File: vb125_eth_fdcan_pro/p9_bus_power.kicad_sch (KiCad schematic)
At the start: 44 parts, among them T2 750315125, U14 LV14360SDDAR, U15 LT8304IS8E#PBF

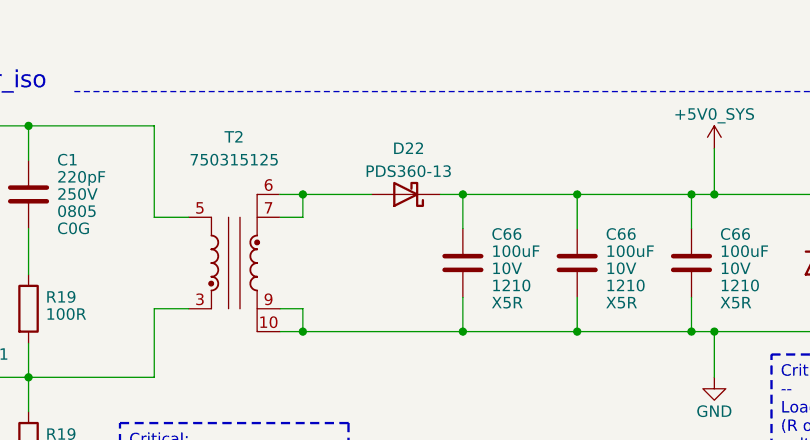
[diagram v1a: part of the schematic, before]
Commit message: Preliminary placement.
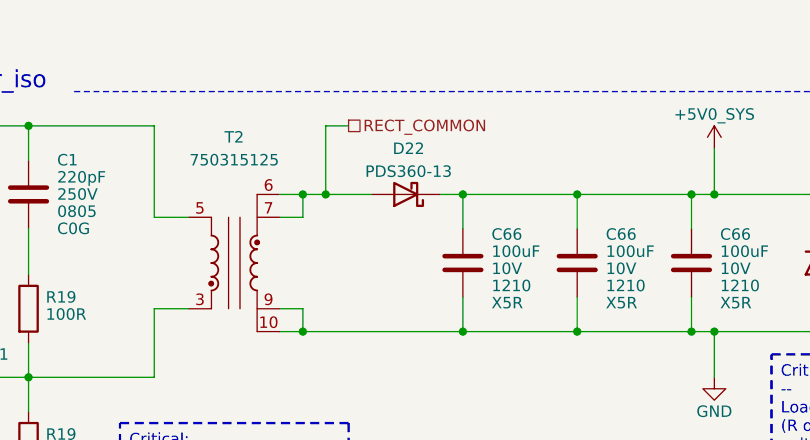
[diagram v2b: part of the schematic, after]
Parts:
- C66, D22: Variant bp_iso -> bp_iso or poe
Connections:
- net RECT_COMMON: now reaches D22.2 (A), T2.6, T2.7
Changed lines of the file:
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@@
   (junction (at 200.66 110.49) (diameter 0) (color 0 0 0 0)
+  )
+  (junction (at 254 73.66) (diameter 0) (color 0 0 0 0)
   )
   (junction (at 251.46 73.66) (diameter 0) (color 0 0 0 0)
@@
     (stroke (width 0) (type default))
   )
+  (wire (pts (xy 254 73.66) (xy 259.08 73.66))
+    (stroke (width 0) (type default))
+  )
   (wire (pts (xy 209.55 110.49) (xy 209.55 119.38))
     (stroke (width 0) (type default))
@@
     (stroke (width 0) (type default))
   )
+  (wire (pts (xy 256.54 66.04) (xy 254 66.04))
+    (stroke (width 0) (type default))
+  )
   (wire (pts (xy 281.94 88.9) (xy 269.24 88.9))
     (stroke (width 0) (type default))
@@
     (stroke (width 0) (type default))
   )
-  (wire (pts (xy 251.46 73.66) (xy 259.08 73.66))
+  (wire (pts (xy 251.46 73.66) (xy 254 73.66))
     (stroke (width 0) (type default))
   )
@@
   )
   (wire (pts (xy 251.46 86.36) (xy 251.46 88.9))
+    (stroke (width 0) (type default))
+  )
+  (wire (pts (xy 254 66.04) (xy 254 73.66))
     (stroke (width 0) (type default))
   )
@@
     (effects (font (size 1.27 1.27)) (justify right))
   )
+  (hierarchical_label "RECT_COMMON" (shape passive) (at 256.54 66.04 0) (fields_autoplaced)
+    (effects (font (size 1.27 1.27)) (justify left))
+    (property "Intersheetrefs" "${INTERSHEET_REFS}" (at 272.123 66.04 0)
+      (effects (font (size 1.27 1.27)) (justify left) hide)
+    )
+  )
   (symbol (lib_id "vhrd_power:+5V0_SYS") (at 297.18 68.58 0) (unit 1)
     (in_bom yes) (on_board yes) (dnp no) (fields_autoplaced)
@@
       (effects (font (size 1.27 1.27)) hide)
     )
-    (property "Variant" "bp_iso" (at 262.89 73.66 0)
+    (property "Variant" "bp_iso or poe" (at 262.89 73.66 0)
       (effects (font (size 1.27 1.27)) hide)
     )
@@
       (effects (font (size 1.27 1.27)) (justify left))
     )
-    (property "Variant" "bp_iso" (at 294.64 81.28 0)
+    (property "Variant" "bp_iso or poe" (at 294.64 81.28 0)
       (effects (font (size 1.27 1.27)) hide)
     )
@@
       (effects (font (size 1.27 1.27)) (justify left))
     )
-    (property "Variant" "bp_iso" (at 281.94 81.28 0)
+    (property "Variant" "bp_iso or poe" (at 281.94 81.28 0)
       (effects (font (size 1.27 1.27)) hide)
     )
@@
       (effects (font (size 1.27 1.27)) (justify left))
     )
-    (property "Variant" "bp_iso" (at 269.24 81.28 0)
-      (effects (font (size 1.27 1.27)) hide)
-    )
+    (property "Variant" "bp_iso or poe" (at 269.24 81.28 0)
+      (effects (font (size 1.27 1.27)) hide)
+    )

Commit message: Floorplan work.
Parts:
- removed C1, C2, C20: 100nF, Capacitor_SMD:C_0402_1005Metric, symbol Device:C
- removed C63: 10uF, Capacitor_SMD:C_1210_3225Metric, symbol Device:C
- removed C66: 100uF, Capacitor_SMD:C_1210_3225Metric, symbol Device:C
- removed D21: PDS360-13, Diode_SMD:D_PowerDI-5, symbol Device:D_Schottky
- removed JP1: Jumper board, vhrd_generic:PCB_JUMPER, symbol Jumper:SolderJumper_2_Open
- removed L6: LMLP07A7M8R2DTAS, vhrd_inductor:LMLP07A7, symbol Device:L_Iron
- removed R19 (x2): 10K, Resistor_SMD:R_0402_1005Metric, symbol Device:R
- removed R19: 57K6, Resistor_SMD:R_0402_1005Metric, symbol Device:R
- removed R19: 49K9, Resistor_SMD:R_0402_1005Metric, symbol Device:R
- removed TP1: TestPoint_Probe, TestPoint:TestPoint_Pad_D1.5mm, symbol Connector:TestPoint_Probe
- removed U14: LV14360SDDAR, Package_SO:SOIC-8-1EP_3.9x4.9mm_P1.27mm_EP2.95x4.9mm_Mask2.71x3.4mm_ThermalVias, symbol vhrd_pmic_regulator:LV14360SDDAR
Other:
- note removed: "Buck"
- note removed: "variant: buspower_dc"

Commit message: Finish layout.
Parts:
- removed TP1 (x2): TestPoint_Probe, TestPoint:TestPoint_Pad_D1.5mm, symbol Connector:TestPoint_Probe
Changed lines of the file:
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@@
   (junction (at 281.94 88.9) (diameter 0) (color 0 0 0 0)
   )
-  (junction (at 210.82 107.95) (diameter 0) (color 0 0 0 0)
-  )
   (junction (at 158.75 116.84) (diameter 0) (color 0 0 0 0)
   )
@@
   (junction (at 220.98 66.04) (diameter 0) (color 0 0 0 0)
   )
-  (junction (at 210.82 93.98) (diameter 0) (color 0 0 0 0)
-  )
   (junction (at 294.64 88.9) (diameter 0) (color 0 0 0 0)
   )
@@
     (stroke (width 0) (type default))
   )
-  (wire (pts (xy 210.82 107.95) (xy 220.98 107.95))
-    (stroke (width 0) (type default))
-  )
   (wire (pts (xy 297.18 88.9) (xy 294.64 88.9))
     (stroke (width 0) (type default))
@@
     (stroke (width 0) (type default))
   )
-  (wire (pts (xy 191.77 107.95) (xy 210.82 107.95))
+  (wire (pts (xy 191.77 107.95) (xy 220.98 107.95))
     (stroke (width 0) (type default))
   )
@@
     (stroke (width 0) (type default))
   )
-  (wire (pts (xy 196.85 93.98) (xy 210.82 93.98))
-    (stroke (width 0) (type default))
-  )
   (wire (pts (xy 115.57 110.49) (xy 115.57 129.54))
     (stroke (width 0) (type default))
@@
     (stroke (width 0) (type default))
   )
-  (wire (pts (xy 210.82 93.98) (xy 220.98 93.98))
+  (wire (pts (xy 196.85 93.98) (xy 220.98 93.98))
     (stroke (width 0) (type default))
   )
@@
         (path "/b473bccb-f14c-41d5-b473-137d3ef8ae1e/2334f909-fe66-4647-954f-aa86c22b7af3"
           (reference "#PWR0196") (unit 1)
-        )
-      )
-    )
-  )
-  (symbol (lib_id "Connector:TestPoint_Probe") (at 210.82 107.95 0) (unit 1)
-    (in_bom yes) (on_board yes) (dnp no)
-    (property "Reference" "TP1" (at 217.17 105.41 0)
-      (effects (font (size 1.27 1.27)))
-    )
-    (property "Value" "TestPoint_Probe" (at 223.52 108.2675 0)
-      (effects (font (size 1.27 1.27)) hide)
-    )
-    (property "Footprint" "TestPoint:TestPoint_Pad_D1.5mm" (at 215.9 107.95 0)
-      (effects (font (size 1.27 1.27)) hide)
-    )
-    (property "Datasheet" "~" (at 215.9 107.95 0)
-      (effects (font (size 1.27 1.27)) hide)
-    )
-    (pin "1")
-    (instances
-      (project "vb125_eth_fdcan_pro"
-        (path "/b473bccb-f14c-41d5-b473-137d3ef8ae1e/c16e79c7-955f-4686-8fe9-acff02e57751"
-          (reference "TP1") (unit 1)
-        )
-        (path "/b473bccb-f14c-41d5-b473-137d3ef8ae1e/13d04be1-6d05-4847-9c03-a8fbeeb3fd19"
-          (reference "TP6") (unit 1)
-        )
-        (path "/b473bccb-f14c-41d5-b473-137d3ef8ae1e/6eaf8f36-f4c1-413f-846c-b502b7be2b8c"
-          (reference "TP14") (unit 1)
-        )
-        (path "/b473bccb-f14c-41d5-b473-137d3ef8ae1e/5caca214-bd98-4d53-9e0b-a904082b09c6"
-          (reference "TP23") (unit 1)
-        )
-        (path "/b473bccb-f14c-41d5-b473-137d3ef8ae1e/2334f909-fe66-4647-954f-aa86c22b7af3"
-          (reference "TP39") (unit 1)
         )
       )
@@
         )
       )
-    )
-  )
-  (symbol (lib_id "Connector:TestPoint_Probe") (at 210.82 93.98 0) (unit 1)
-    (in_bom yes) (on_board yes) (dnp no)
-    (property "Reference" "TP1" (at 217.17 91.44 0)
-      (effects (font (size 1.27 1.27)))
-    )
-    (property "Value" "TestPoint_Probe" (at 223.52 94.2975 0)
-      (effects (font (size 1.27 1.27)) hide)
-    )
-    (property "Footprint" "TestPoint:TestPoint_Pad_D1.5mm" (at 215.9 93.98 0)
-      (effects (font (size 1.27 1.27)) hide)
-    )
-    (property "Datasheet" "~" (at 215.9 93.98 0)
-      (effects (font (size 1.27 1.27)) hide)
-    )
-    (pin "1")
-    (instances
-      (project "vb125_eth_fdcan_pro"
-        (path "/b473bccb-f14c-41d5-b473-137d3ef8ae1e/c16e79c7-955f-4686-8fe9-acff02e57751"
-          (reference "TP1") (unit 1)
-        )
-        (path "/b473bccb-f14c-41d5-b473-137d3ef8ae1e/13d04be1-6d05-4847-9c03-a8fbeeb3fd19"
-          (reference "TP6") (unit 1)
-        )
-        (path "/b473bccb-f14c-41d5-b473-137d3ef8ae1e/6eaf8f36-f4c1-413f-846c-b502b7be2b8c"
-          (reference "TP14") (unit 1)
-        )
-        (path "/b473bccb-f14c-41d5-b473-137d3ef8ae1e/5caca214-bd98-4d53-9e0b-a904082b09c6"
-          (reference "TP23") (unit 1)
-        )
-        (path "/b473bccb-f14c-41d5-b473-137d3ef8ae1e/2334f909-fe66-4647-954f-aa86c22b7af3"
-          (reference "TP38") (unit 1)
-        )
-      )

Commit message: Update sch and pcb.
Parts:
- added E5: SparkGap, vhrd_generic:SPARK_GAP_011, symbol Device:SparkGap
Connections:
- net +VIN_DB9: now also E5.1
- net CHASSIS: now also E5.2
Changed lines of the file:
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@@
   (junction (at 281.94 88.9) (diameter 0) (color 0 0 0 0)
+  )
+  (junction (at 68.58 66.04) (diameter 0) (color 0 0 0 0)
   )
   (junction (at 158.75 116.84) (diameter 0) (color 0 0 0 0)
@@
     (stroke (width 0) (type default))
   )
+  (wire (pts (xy 68.58 66.04) (xy 77.47 66.04))
+    (stroke (width 0) (type default))
+  )
+  (wire (pts (xy 68.58 66.04) (xy 68.58 67.31))
+    (stroke (width 0) (type default))
+  )
   (wire (pts (xy 115.57 110.49) (xy 115.57 129.54))
     (stroke (width 0) (type default))
@@
     (stroke (width 0) (type default))
   )
-  (wire (pts (xy 74.93 66.04) (xy 77.47 66.04))
+  (wire (pts (xy 60.96 66.04) (xy 68.58 66.04))
     (stroke (width 0) (type default))
   )
@@
   )
   (wire (pts (xy 254 66.04) (xy 254 73.66))
+    (stroke (width 0) (type default))
+  )
+  (wire (pts (xy 68.58 77.47) (xy 68.58 78.74))
     (stroke (width 0) (type default))
   )
@@
     (effects (font (size 1.27 1.27)) (justify left bottom))
   )
-  (hierarchical_label "+VIN_DB9" (shape input) (at 74.93 66.04 180) (fields_autoplaced)
+  (hierarchical_label "+VIN_DB9" (shape input) (at 60.96 66.04 180) (fields_autoplaced)
     (effects (font (size 1.27 1.27)) (justify right))
   )
@@
   (symbol (lib_id "Device:D_TVS") (at 77.47 72.39 270) (mirror x) (unit 1)
     (in_bom yes) (on_board yes) (dnp no)
-    (property "Reference" "D21" (at 63.5 72.39 0)
-      (effects (font (size 1.27 1.27)))
-    )
-    (property "Value" "buspower_iso: SMAJ58CA; buspower_dc: SMAJ36CA" (at 66.04 95.25 0)
+    (property "Reference" "D21" (at 59.69 72.39 0)
+      (effects (font (size 1.27 1.27)))
+    )
+    (property "Value" "buspower_iso: SMAJ58CA; buspower_dc: SMAJ36CA" (at 62.23 95.25 0)
       (effects (font (size 1.27 1.27)))
     )
@@
     )
   )
+  (symbol (lib_id "Device:SparkGap") (at 68.58 72.39 270) (unit 1)
+    (in_bom yes) (on_board yes) (dnp no)
+    (property "Reference" "E5" (at 67.31 60.96 90)
+      (effects (font (size 1.27 1.27)))
+    )
+    (property "Value" "SparkGap" (at 68.58 63.5 90)
+      (effects (font (size 1.27 1.27)))
+    )
+    (property "Footprint" "vhrd_generic:SPARK_GAP_011" (at 66.802 72.39 0)
+      (effects (font (size 1.27 1.27)) hide)
+    )
+    (property "Datasheet" "~" (at 68.58 72.39 90)
+      (effects (font (size 1.27 1.27)) hide)
+    )
+    (pin "1")
+    (pin "2")
+    (instances
+      (project "vb125_eth_fdcan_pro"
+        (path "/b473bccb-f14c-41d5-b473-137d3ef8ae1e/96773d61-2940-42cb-9a0c-01cb58b4a4b5"
+          (reference "E5") (unit 1)
+        )
+        (path "/b473bccb-f14c-41d5-b473-137d3ef8ae1e/1ac386c6-64ba-4865-8e07-7f3718b45cdc"
+          (reference "E6") (unit 1)
+        )
+        (path "/b473bccb-f14c-41d5-b473-137d3ef8ae1e/2334f909-fe66-4647-954f-aa86c22b7af3"
+          (reference "E5") (unit 1)
+        )
+      )
+    )
+  )
   (symbol (lib_id "Device:C") (at 104.14 106.68 0) (unit 1)
     (in_bom yes) (on_board yes) (dnp no)
@@
         )
       )
+    )
+  )
+  (symbol (lib_id "vhrd_power:CHASSIS") (at 68.58 78.74 0) (mirror y) (unit 1)
+    (in_bom yes) (on_board yes) (dnp no) (fields_autoplaced)
+    (property "Reference" "#PWR0153" (at 68.58 85.09 0)
+      (effects (font (size 1.27 1.27)) hide)
+    )
+    (property "Value" "CHASSIS" (at 68.58 83.82 0)
+      (effects (font (size 1.27 1.27)))
+    )
+    (property "Footprint" "" (at 68.58 78.74 0)
+      (effects (font (size 1.27 1.27)) hide)
+    )
+    (property "Datasheet" "~" (at 68.58 78.74 0)
+      (effects (font (size 1.27 1.27)) hide)
+    )
+    (pin "1")
+    (instances
+      (project "vb125_eth_fdcan_pro"
+        (path "/b473bccb-f14c-41d5-b473-137d3ef8ae1e/13d04be1-6d05-4847-9c03-a8fbeeb3fd19"
+          (reference "#PWR0153") (unit 1)
+        )
+        (path "/b473bccb-f14c-41d5-b473-137d3ef8ae1e/96773d61-2940-42cb-9a0c-01cb58b4a4b5"
+          (reference "#PWR0165") (unit 1)
+        )
+        (path "/b473bccb-f14c-41d5-b473-137d3ef8ae1e/2334f909-fe66-4647-954f-aa86c22b7af3"
+          (reference "#PWR0181") (unit 1)
+        )
+      )

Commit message: Update outline.
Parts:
- D18, D20: footprint Diode_SMD:D_SOD-123F -> vhrd_diode:D_SOD-123F
- D19, D21: footprint Diode_SMD:D_SMA -> vhrd_diode:D_SMA
- D23: footprint Diode_SMD:D_SOD-323 -> vhrd_diode:D_SOD-323
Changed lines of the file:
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@@
       (effects (font (size 1.27 1.27)) (justify right))
     )
-    (property "Footprint" "Diode_SMD:D_SMA" (at 196.85 73.66 0)
+    (property "Footprint" "vhrd_diode:D_SMA" (at 196.85 73.66 0)
       (effects (font (size 1.27 1.27)) hide)
     )
@@
       (effects (font (size 1.27 1.27)))
     )
-    (property "Footprint" "Diode_SMD:D_SOD-323" (at 308.61 81.28 0)
+    (property "Footprint" "vhrd_diode:D_SOD-323" (at 308.61 81.28 0)
       (effects (font (size 1.27 1.27)) hide)
     )
@@
       (effects (font (size 1.27 1.27)))
     )
-    (property "Footprint" "Diode_SMD:D_SMA" (at 77.47 72.39 0)
+    (property "Footprint" "vhrd_diode:D_SMA" (at 77.47 72.39 0)
       (effects (font (size 1.27 1.27)) hide)
     )
@@
       (effects (font (size 1.27 1.27)) (justify left))
     )
-    (property "Footprint" "Diode_SMD:D_SOD-123F" (at 196.85 86.36 0)
+    (property "Footprint" "vhrd_diode:D_SOD-123F" (at 196.85 86.36 0)
       (effects (font (size 1.27 1.27)) hide)
     )
@@
       (effects (font (size 1.27 1.27)) (justify right))
     )
-    (property "Footprint" "Diode_SMD:D_SOD-123F" (at 86.36 66.04 0)
-      (effects (font (size 1.27 1.27)) hide)
-    )
+    (property "Footprint" "vhrd_diode:D_SOD-123F" (at 86.36 66.04 0)
+      (effects (font (size 1.27 1.27)) hide)
+    )
